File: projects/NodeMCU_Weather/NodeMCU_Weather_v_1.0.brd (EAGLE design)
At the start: 100 x 80 mm, 4 parts

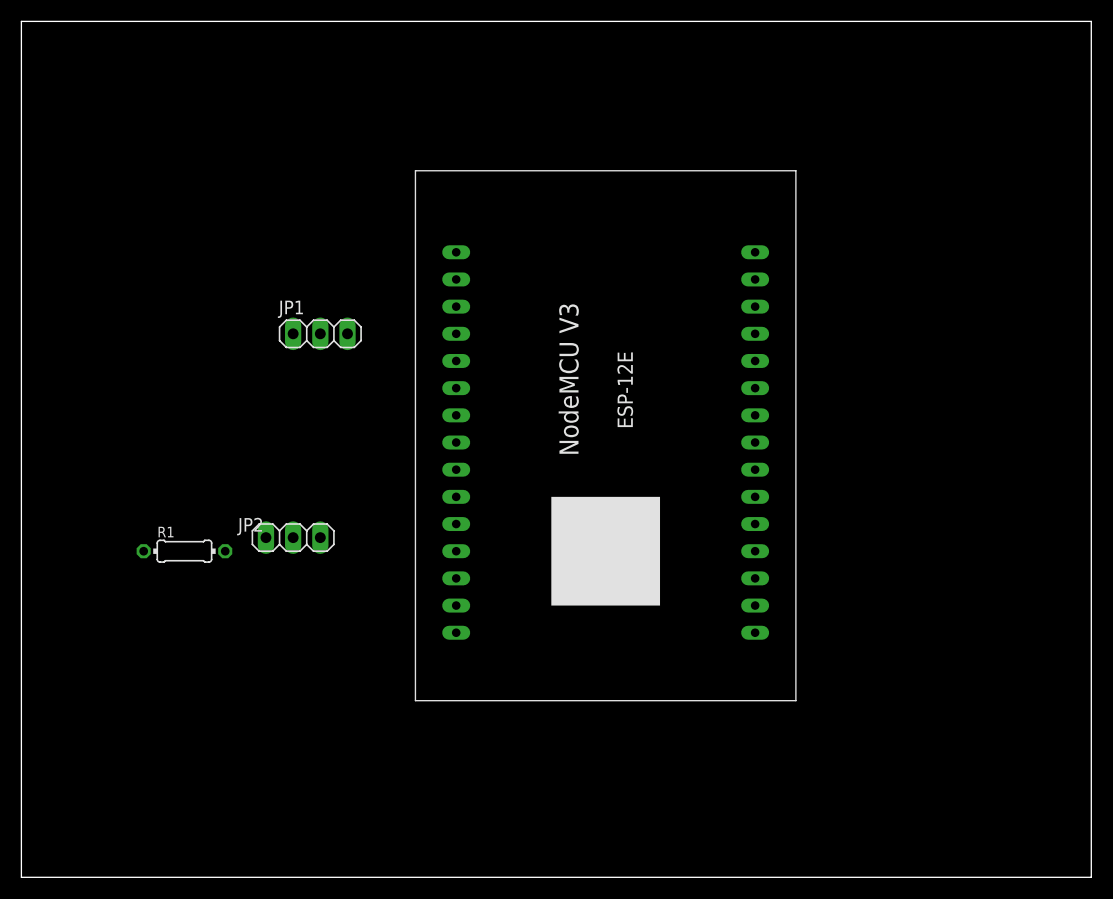
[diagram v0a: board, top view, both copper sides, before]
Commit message: Base of nodemcu schematics and board
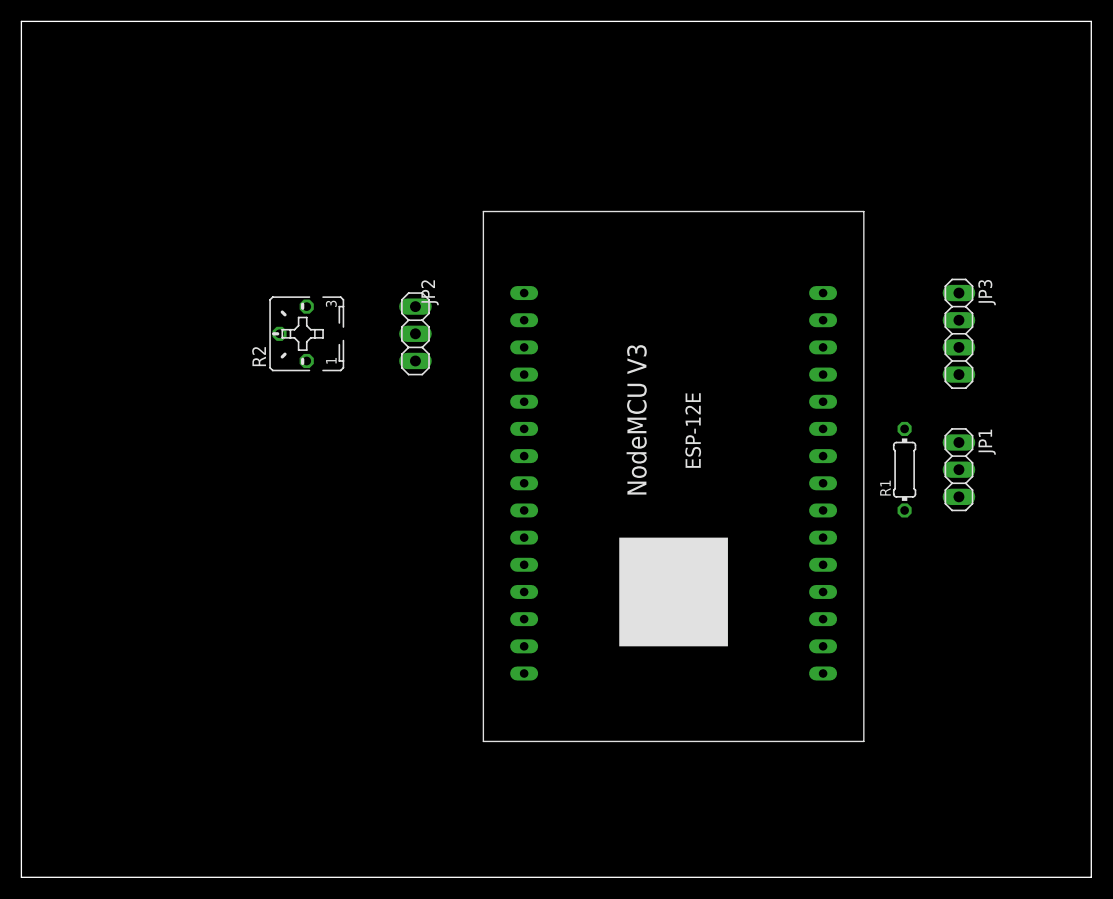
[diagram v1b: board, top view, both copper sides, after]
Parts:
- added JP3: SSD1306, pinhead:1X04
- added R2: (no value), pot:B25P
- JP1: value (none) -> DS18B20
- JP2: value (none) -> SunSensor
- moved R1 67.7 mm to (82.5, 38.1), turned to 90 degrees
- moved JP1 61.0 mm to (87.6, 38.1), turned to 270 degrees
- moved JP2 22.2 mm to (36.8, 50.8), turned to 270 degrees
- moved U$1 7.41 mm to (57.1, 39.4)
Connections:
- new net 0: JP1.3, JP2.3, JP3.4, U$1.14, U$1.17, U$1.21, U$1.7
- new net DS: JP1.2, R1.1
- new net N$2: JP2.1, R2.E
- new net OLED_SCL: JP3.2
- new net OLED_SDA: JP3.1
- new net SUN_ADC: JP2.2
- new net VCC: JP1.1, JP3.3, R1.2, R2.S, U$1.20, U$1.6
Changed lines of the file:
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@@
 </autorouter>
 <elements>
-<element name="JP1" library="pinhead" library_urn="urn:adsk.eagle:library:325" package="1X03" package3d_urn="urn:adsk.eagle:package:22458/2" value="" x="27.94" y="50.8" smashed="yes">
-<attribute name="NAME" x="24.0538" y="52.6288" size="1.27" layer="25" ratio="10"/>
-<attribute name="POPULARITY" value="92" x="45.72" y="-2.54" size="1.778" layer="27" display="off"/>
-<attribute name="VALUE" x="24.13" y="47.625" size="1.27" layer="27"/>
+<element name="JP1" library="pinhead" library_urn="urn:adsk.eagle:library:325" package="1X03" package3d_urn="urn:adsk.eagle:package:22458/2" value="DS18B20" x="87.63" y="38.1" smashed="yes" rot="R270">
+<attribute name="NAME" x="89.4588" y="41.9862" size="1.27" layer="25" ratio="10" rot="R270"/>
+<attribute name="POPULARITY" value="92" x="34.29" y="20.32" size="1.778" layer="27" rot="R270" display="off"/>
+<attribute name="VALUE" x="84.455" y="41.91" size="1.27" layer="27" rot="R270"/>
 </element>
-<element name="JP2" library="pinhead" library_urn="urn:adsk.eagle:library:325" package="1X03" package3d_urn="urn:adsk.eagle:package:22458/2" value="" x="25.4" y="31.75" smashed="yes">
-<attribute name="NAME" x="20.2438" y="32.3088" size="1.27" layer="25" ratio="10"/>
-<attribute name="POPULARITY" value="92" x="52.07" y="-21.59" size="1.778" layer="27" display="off"/>
-<attribute name="VALUE" x="21.59" y="28.575" size="1.27" layer="27"/>
+<element name="JP2" library="pinhead" library_urn="urn:adsk.eagle:library:325" package="1X03" package3d_urn="urn:adsk.eagle:package:22458/2" value="SunSensor" x="36.83" y="50.8" smashed="yes" rot="R270">
+<attribute name="NAME" x="37.3888" y="55.9562" size="1.27" layer="25" ratio="10" rot="R270"/>
+<attribute name="POPULARITY" value="92" x="-16.51" y="24.13" size="1.778" layer="27" rot="R270" display="off"/>
+<attribute name="VALUE" x="33.655" y="54.61" size="1.27" layer="27" rot="R270"/>
 </element>
-<element name="R1" library="eagle-ltspice" library_urn="urn:adsk.eagle:library:217" package="0204/7" package3d_urn="urn:adsk.eagle:package:13274/1" value="" x="15.24" y="30.48" smashed="yes">
-<attribute name="NAME" x="12.7" y="31.7754" size="0.9906" layer="25" ratio="10"/>
-<attribute name="SPICEMODEL" value="NONE" x="52.07" y="-21.59" size="1.778" layer="27" display="off"/>
-<attribute name="SPICEPREFIX" value="R" x="52.07" y="-21.59" size="1.778" layer="27" display="off"/>
-<attribute name="VALUE" x="13.6144" y="29.9974" size="0.9906" layer="27" ratio="10"/>
+<element name="R1" library="eagle-ltspice" library_urn="urn:adsk.eagle:library:217" package="0204/7" package3d_urn="urn:adsk.eagle:package:13274/1" value="" x="82.55" y="38.1" smashed="yes" rot="R90">
+<attribute name="NAME" x="81.2546" y="35.56" size="0.9906" layer="25" ratio="10" rot="R90"/>
+<attribute name="SPICEMODEL" value="NONE" x="134.62" y="74.93" size="1.778" layer="27" rot="R90" display="off"/>
+<attribute name="SPICEPREFIX" value="R" x="134.62" y="74.93" size="1.778" layer="27" rot="R90" display="off"/>
+<attribute name="VALUE" x="83.0326" y="36.4744" size="0.9906" layer="27" ratio="10" rot="R90"/>
 </element>
-<element name="U$1" library="NODEMCU" package="NODEMCUESP8266" value="" x="50.8" y="43.18" smashed="yes"/>
+<element name="U$1" library="NODEMCU" package="NODEMCUESP8266" value="" x="57.15" y="39.37" smashed="yes"/>
+<element name="JP3" library="pinhead" library_urn="urn:adsk.eagle:library:325" package="1X04" package3d_urn="urn:adsk.eagle:package:22407/2" value="SSD1306" x="87.63" y="50.8" smashed="yes" rot="R270">
+<attribute name="NAME" x="89.4588" y="55.9562" size="1.27" layer="25" ratio="10" rot="R270"/>
+<attribute name="POPULARITY" value="91" x="87.63" y="50.8" size="1.778" layer="27" rot="R270" display="off"/>
+<attribute name="VALUE" x="84.455" y="55.88" size="1.27" layer="27" rot="R270"/>
+</element>
+<element name="R2" library="pot" library_urn="urn:adsk.eagle:library:331" package="B25P" package3d_urn="urn:adsk.eagle:package:22684/1" value="" x="26.67" y="50.8" smashed="yes" rot="R90">
+<attribute name="NAME" x="22.86" y="47.625" size="1.27" layer="25" ratio="10" rot="R90"/>
+<attribute name="POPULARITY" value="7" x="26.67" y="50.8" size="1.778" layer="27" rot="R90" display="off"/>
+<attribute name="VALUE" x="31.75" y="47.6504" size="1.27" layer="27" ratio="10" rot="R90"/>
+</element>
 </elements>
 <signals>
+<signal name="0">
+<contactref element="U$1" pad="7"/>
+<contactref element="JP1" pad="3"/>
+<contactref element="JP3" pad="4"/>
+<contactref element="JP2" pad="3"/>
+<contactref element="U$1" pad="17"/>
+<contactref element="U$1" pad="14"/>
+<contactref element="U$1" pad="21"/>
+<wire x1="87.63" y1="35.56" x2="87.63" y2="46.99" width="0" layer="19" extent="1-1"/>
+<wire x1="74.93" y1="39.37" x2="87.63" y2="35.56" width="0" layer="19" extent="1-1"/>
+<wire x1="74.93" y1="21.59" x2="74.93" y2="39.37" width="0" layer="19" extent="1-1"/>
+<wire x1="46.99" y1="21.59" x2="74.93" y2="21.59" width="0" layer="19" extent="1-1"/>
+<wire x1="46.99" y1="31.75" x2="46.99" y2="21.59" width="0" layer="19" extent="1-1"/>
+<wire x1="36.83" y1="48.26" x2="46.99" y2="31.75" width="0" layer="19" extent="1-1"/>
+</signal>
+<signal name="VCC">
+<contactref element="U$1" pad="6"/>
+<contactref element="JP1" pad="1"/>
+<contactref element="R1" pad="2"/>
+<contactref element="JP3" pad="3"/>
+<contactref element="R2" pad="S"/>
+<contactref element="U$1" pad="20"/>
+<wire x1="87.63" y1="40.64" x2="87.63" y2="49.53" width="0" layer="19" extent="1-1"/>
+<wire x1="82.55" y1="41.91" x2="87.63" y2="40.64" width="0" layer="19" extent="1-1"/>
+<wire x1="74.93" y1="41.91" x2="82.55" y2="41.91" width="0" layer="19" extent="1-1"/>
+<wire x1="46.99" y1="29.21" x2="74.93" y2="41.91" width="0" layer="19" extent="1-1"/>
+<wire x1="24.13" y1="50.8" x2="46.99" y2="29.21" width="0" layer="19" extent="1-1"/>
+</signal>
+<signal name="DS">
+<contactref element="R1" pad="1"/>
+<contactref element="JP1" pad="2"/>
+<wire x1="82.55" y1="34.29" x2="87.63" y2="38.1" width="0" layer="19" extent="1-1"/>
+</signal>
+<signal name="OLED_SDA">
+<contactref element="JP3" pad="1"/>
+</signal>
+<signal name="OLED_SCL">
+<contactref element="JP3" pad="2"/>
+</signal>
+<signal name="SUN_ADC">
+<contactref element="JP2" pad="2"/>
+</signal>
+<signal name="N$2">
+<contactref element="R2" pad="E"/>
+<contactref element="JP2" pad="1"/>
+<wire x1="26.67" y1="53.34" x2="36.83" y2="53.34" width="0" layer="19" extent="1-1"/>
+</signal>
 </signals>
 <mfgpreviewcolors>
